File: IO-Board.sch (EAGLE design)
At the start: 59 parts, among them IC1 PCF8574P, IC2 PCF8574P

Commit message: IO-Board angepasst, 433MHz-Sender hinzugefügt
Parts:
- added +3V3.1, +3V3.2, +3V3.3, +3V3.4, 1WIRE.1, 1WIRE.2, 1WIRE.3, 1WIRE.4, GND.1, GND.2, GND.3, GND.4, GNDIO.1, GNDIO.10, GNDIO.11, GNDIO.12, GNDIO.13, GNDIO.14, GNDIO.15, GNDIO.16, GNDIO.17, GNDIO.18, GNDIO.19, GNDIO.2, GNDIO.20, GNDIO.21, GNDIO.22, GNDIO.23, GNDIO.24, GNDIO.3, GNDIO.4, GNDIO.5, GNDIO.6, GNDIO.7, GNDIO.8, GNDIO.9, GPIO_06, GPIO_12, GPIO_13, GPIO_16, GPIO_17, GPIO_18, GPIO_19, GPIO_20, GPIO_21, GPIO_22, GPIO_23, IC3_INT, IC4_INT, J1.1, J1.2, J1.3, J1.4, J1.5, J1.6, J1.7, J1.8, J2.1, J2.2, J2.3, J2.4, J2.5, J2.6, J2.7, J2.8, J3.1, J3.2, J3.3, J3.4, J3.5, J3.6, J3.7, J3.8, J4.1, J4.2, J4.3, J4.4, J4.5, J4.6, J4.7, J4.8, SV2.1, SV2.10, SV2.2, SV2.3, SV2.4, SV2.5, SV2.6, SV2.7, SV2.8, SV2.9, SV3.1, SV3.10, SV3.2, SV3.3, SV3.4, SV3.5, SV3.6, SV3.7, SV3.8, SV3.9, TP17, TP18, TP19, TP20, TP21, TP22, TP23, TP24, TP26, TP27, TP28, TP29, TP30, TP31, TP32, TP33, VCCIO.1, VCCIO.10, VCCIO.11, VCCIO.12, VCCIO.13, VCCIO.14, VCCIO.15, VCCIO.16, VCCIO.17, VCCIO.18, VCCIO.19, VCCIO.2, VCCIO.20, VCCIO.21, VCCIO.22, VCCIO.23, VCCIO.24, VCCIO.3, VCCIO.4, VCCIO.5, VCCIO.6, VCCIO.7, VCCIO.8, VCCIO.9: TPPAD1-13, testpad:TPPAD1-13
- added C3, C4: 100nF, rcl:C-EU025-025X050
- added IC3, IC4: PCF8574P, micro-philips:PCF8574P
- added J1, J2, J3, J4: (no value), con-amp:555141-1
- added J5: J7MM, jumper:J7MM
- added OK1, OK10, OK11, OK12, OK13, OK14, OK15, OK16, OK17, OK18, OK19, OK2, OK20, OK21, OK22, OK23, OK24, OK25, OK26, OK27, OK28, OK29, OK3, OK30, OK31, OK32, OK4, OK5, OK6, OK7, OK8, OK9: CNY17SMD, homepi:CNY17SMD
- added R17, R20, R23, R26, R29, R32, R35, R38, R41, R44, R47: 10k, rcl:R-EU_0204/2V
- added R18, R21, R24, R27, R30, R33, R36, R39, R42, R45, R48: 4k7, rcl:R-EU_0204/2V
- added R19, R22, R25, R28, R31, R34, R37, R40, R43, R46, R49, R50, R51, R52, R53, R54, R55, R56, R57, R58, R59, R60, R61, R62, R63, R64: 330, rcl:R-EU_0204/2V
- added R65, R66: J5MM, jumper:J5MM
- added SJ10, SJ11, SJ12, SJ7, SJ8, SJ9: (no value), jumper:SJ2W
- added SV2, SV3: (no value), con-harting-ml:ML10
- R1, R10, R13, R16, R4, R7: value (none) -> 330
- R11, R14, R2, R5, R8: value (none) -> 10k
- R12, R15, R3, R6, R9: value (none) -> 4k7
- T1, T10, T11, T12, T13, T14, T15, T16, T2, T3, T4, T5, T6, T7, T8, T9: value (none) -> BC337-25; device transistor:BC557C-PNP-TO92-EBC -> transistor:BC337-25-NPN-TO92-CBE
- TP1, TP10, TP11, TP12, TP13, TP14, TP15, TP16, TP2, TP3, TP4, TP5, TP6, TP7, TP8, TP9: value TPPAD1-17 -> TPPAD1-13; device testpad:TPPAD1-17 -> testpad:TPPAD1-13
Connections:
- removed net +5V: SV1.1
- new net 1WIRE: 1WIRE.1.TP, 1WIRE.2.TP, 1WIRE.3.TP, 1WIRE.4.TP, J5.2
- new net GNDIO: GNDIO.1.TP, GNDIO.10.TP, GNDIO.11.TP, GNDIO.12.TP, GNDIO.13.TP, GNDIO.14.TP, GNDIO.15.TP, GNDIO.16.TP, GNDIO.17.TP, GNDIO.18.TP, GNDIO.19.TP, GNDIO.2.TP, GNDIO.20.TP, GNDIO.21.TP, GNDIO.22.TP, GNDIO.23.TP, GNDIO.24.TP, GNDIO.3.TP, GNDIO.4.TP, GNDIO.5.TP, GNDIO.6.TP, GNDIO.7.TP, GNDIO.8.TP, GNDIO.9.TP, J1.S1, J1.S2, J2.S1, J2.S2, J3.S1, J3.S2, J4.S1, J4.S2, R11.1, R14.1, R17.1, R2.1, R20.1, R23.1, R26.1, R29.1, R32.1, R35.1, R38.1, R41.1, R44.1, R47.1, R5.1, R8.1, SV1.30, T1.E, T10.E, T11.E, T12.E, T13.E, T14.E, T15.E, T16.E, T2.E, T3.E, T4.E, T5.E, T6.E, T7.E, T8.E, T9.E
- new net IN_1.0: IC3.P0, OK17.COL
- new net IN_1.1: IC3.P1, OK18.COL
- new net IN_1.2: IC3.P2, OK19.COL
- new net IN_1.3: IC3.P3, OK20.COL
- new net IN_1.4: IC3.P4, OK21.COL
- new net IN_1.5: IC3.P5, OK22.COL
- new net IN_1.6: IC3.P6, OK23.COL
- new net IN_1.7: IC3.P7, OK24.COL
- new net IN_2.0: IC4.P0, OK25.COL
- new net IN_2.1: IC4.P1, OK26.COL
- new net IN_2.2: IC4.P2, OK27.COL
- new net IN_2.3: IC4.P3, OK28.COL
- new net IN_2.4: IC4.P4, OK29.COL
- new net IN_2.5: IC4.P5, OK30.COL
- new net IN_2.6: IC4.P6, OK31.COL
- new net IN_2.7: IC4.P7, OK32.COL
- new net N$100: OK22.A, R54.1
- new net N$101: OK22.C, TP22.TP
- new net N$102: OK23.A, R55.1
- new net N$103: OK23.C, TP23.TP
- new net N$104: OK24.A, R56.1
- new net N$105: OK24.C, TP24.TP
- new net N$106: IC3.!INT, IC3_INT.TP
- new net N$107: IC4.A0, SJ10.2
- new net N$108: IC4.A1, SJ11.2
- new net N$109: IC4.A2, SJ12.2
- new net N$110: OK25.A, R57.1
- new net N$111: OK25.C, TP26.TP
- new net N$112: OK26.A, R58.1
- new net N$113: OK26.C, TP27.TP
- new net N$114: OK27.A, R59.1
- new net N$115: OK27.C, TP28.TP
- new net N$116: OK28.A, R60.1
- new net N$117: OK28.C, TP29.TP
- new net N$118: OK29.A, R61.1
- new net N$119: OK29.C, TP30.TP
- new net N$120: OK30.A, R62.1
- new net N$121: OK30.C, TP31.TP
- new net N$122: OK31.A, R63.1
- new net N$123: OK31.C, TP32.TP
- new net N$124: OK32.A, R64.1
- new net N$125: OK32.C, TP33.TP
- new net N$126: IC4.!INT, IC4_INT.TP
- new net N$127: IC4.SDA, R65.1
- new net N$128: IC4.SCL, R66.1
- new net N$129: J3.1, J3.1.TP
- new net N$130: J3.2, J3.2.TP
- new net N$131: J3.3, J3.3.TP
- new net N$132: J3.4, J3.4.TP
- new net N$133: J3.5, J3.5.TP
- new net N$134: J3.6, J3.6.TP
- new net N$135: J3.7, J3.7.TP
- new net N$136: J3.8, J3.8.TP
- new net N$137: J4.1, J4.1.TP
- new net N$138: J4.2, J4.2.TP
- new net N$139: J4.3, J4.3.TP
- new net N$140: J4.4, J4.4.TP
- new net N$141: J4.5, J4.5.TP
- new net N$142: J4.6, J4.6.TP
- new net N$143: J4.7, J4.7.TP
- new net N$144: J4.8, J4.8.TP
- new net N$145: J5.1, SV1.7
- new net N$146: GPIO_23.TP, SV1.25
- new net N$147: GPIO_22.TP, SV1.24
- new net N$148: GPIO_21.TP, SV1.23
- new net N$149: GPIO_20.TP, SV1.22
- new net N$150: GPIO_19.TP, SV1.21
- new net N$151: GPIO_18.TP, SV1.20
- new net N$152: GPIO_17.TP, SV1.19
- new net N$153: GPIO_16.TP, SV1.18
- new net N$154: GPIO_13.TP, SV1.17
- new net N$155: GPIO_12.TP, SV1.16
- new net N$156: GPIO_06.TP, SV1.15
- new net N$157: SV2.1, SV2.1.TP
- new net N$158: SV2.2, SV2.2.TP
- new net N$159: SV2.3, SV2.3.TP
- new net N$160: SV2.4, SV2.4.TP
- new net N$161: SV2.5, SV2.5.TP
- new net N$162: SV2.6, SV2.6.TP
- new net N$163: SV2.7, SV2.7.TP
- new net N$164: SV2.8, SV2.8.TP
- new net N$165: SV2.9, SV2.9.TP
- new net N$166: SV2.10, SV2.10.TP
- new net N$167: SV3.1, SV3.1.TP
- new net N$168: SV3.2, SV3.2.TP
- new net N$169: SV3.3, SV3.3.TP
- new net N$170: SV3.4, SV3.4.TP
- new net N$171: SV3.5, SV3.5.TP
- new net N$172: SV3.6, SV3.6.TP
- new net N$173: SV3.7, SV3.7.TP
- new net N$174: SV3.8, SV3.8.TP
- new net N$175: SV3.9, SV3.9.TP
- new net N$176: SV3.10, SV3.10.TP
- new net N$28: T7.C, TP7.TP
- new net N$29: OK7.A, R19.2
- new net N$30: OK7.EMI, R20.2, R21.1
- new net N$55: R27.2, T9.B
- new net N$56: T10.C, TP10.TP
- new net N$57: OK10.A, R28.2
- new net N$58: OK10.EMI, R29.2, R30.1
- new net N$59: R30.2, T10.B
- new net N$60: T11.C, TP11.TP
- new net N$61: OK11.A, R31.2
- new net N$62: OK11.EMI, R32.2, R33.1
- new net N$63: R33.2, T11.B
- new net N$64: T12.C, TP12.TP
- new net N$65: OK12.A, R34.2
- new net N$66: OK12.EMI, R35.2, R36.1
- new net N$67: R36.2, T12.B
- new net N$68: T13.C, TP13.TP
- new net N$69: OK13.A, R37.2
- new net N$70: OK13.EMI, R38.2, R39.1
- new net N$71: R39.2, T13.B
- new net N$72: T14.C, TP14.TP
- new net N$73: OK14.A, R40.2
- new net N$74: OK14.EMI, R41.2, R42.1
- new net N$75: R42.2, T14.B
- new net N$76: T15.C, TP15.TP
- new net N$77: OK15.A, R43.2
- new net N$78: OK15.EMI, R44.2, R45.1
- new net N$79: R45.2, T15.B
- new net N$80: T16.C, TP16.TP
- new net N$81: OK16.A, R46.2
- new net N$82: OK16.EMI, R47.2, R48.1
- new net N$83: R48.2, T16.B
- new net N$87: IC3.A0, SJ7.2
- new net N$88: IC3.A1, SJ8.2
- new net N$89: IC3.A2, SJ9.2
- new net N$90: OK17.A, R49.1
- new net N$91: OK17.C, TP17.TP
- new net N$92: OK18.A, R50.1
- new net N$93: OK18.C, TP18.TP
- new net N$94: OK19.A, R51.1
- new net N$95: OK19.C, TP19.TP
- new net N$96: OK20.A, R52.1
- new net N$97: OK20.C, TP20.TP
- new net N$98: OK21.A, R53.1
- new net N$99: OK21.C, TP21.TP
- new net OUT_1.0: IC1.P0, OK1.C
- new net OUT_1.1: IC1.P1, OK2.C
- new net OUT_1.2: IC1.P2, OK3.C
- new net OUT_1.3: IC1.P3, OK4.C
- new net OUT_1.4: IC1.P4, OK5.C
- new net OUT_1.5: IC1.P5, OK6.C
- new net OUT_1.6: IC1.P6, OK7.C
- new net OUT_1.7: IC1.P7, OK8.C
- new net OUT_2.0: IC2.P0, OK9.C
- new net OUT_2.1: IC2.P1, OK10.C
- new net OUT_2.2: IC2.P2, OK11.C
- new net OUT_2.3: IC2.P3, OK12.C
- new net OUT_2.4: IC2.P4, OK13.C
- new net OUT_2.5: IC2.P5, OK14.C
- new net OUT_2.6: IC2.P6, OK15.C
- new net OUT_2.7: IC2.P7, OK16.C
- new net VCCIO: OK1.COL, OK10.COL, OK11.COL, OK12.COL, OK13.COL, OK14.COL, OK15.COL, OK16.COL, OK2.COL, OK3.COL, OK4.COL, OK5.COL, OK6.COL, OK7.COL, OK8.COL, OK9.COL, R49.2, R50.2, R51.2, R52.2, R53.2, R54.2, R55.2, R56.2, R57.2, R58.2, R59.2, R60.2, R61.2, R62.2, R63.2, R64.2, SV1.31, VCCIO.1.TP, VCCIO.10.TP, VCCIO.11.TP, VCCIO.12.TP, VCCIO.13.TP, VCCIO.14.TP, VCCIO.15.TP, VCCIO.16.TP, VCCIO.17.TP, VCCIO.18.TP, VCCIO.19.TP, VCCIO.2.TP, VCCIO.20.TP, VCCIO.21.TP, VCCIO.22.TP, VCCIO.23.TP, VCCIO.24.TP, VCCIO.3.TP, VCCIO.4.TP, VCCIO.5.TP, VCCIO.6.TP, VCCIO.7.TP, VCCIO.8.TP, VCCIO.9.TP
- net +3V3: now also +3V3.1.TP, +3V3.2.TP, +3V3.3.TP, +3V3.4.TP, C3.1, C4.1, IC3.VDD, IC4.VDD, R1.1, R10.1, R13.1, R16.1, R19.1, R22.1, R25.1, R28.1, R31.1, R34.1, R37.1, R4.1, R40.1, R43.1, R46.1, R7.1, SJ10.3, SJ11.3, SJ12.3, SJ7.3, SJ8.3, SJ9.3
- net GND: now also C3.2, C4.2, GND.1.TP, GND.2.TP, GND.3.TP, GND.4.TP, IC3.VSS, IC4.VSS, OK17.EMI, OK18.EMI, OK19.EMI, OK20.EMI, OK21.EMI, OK22.EMI, OK23.EMI, OK24.EMI, OK25.EMI, OK26.EMI, OK27.EMI, OK28.EMI, OK29.EMI, OK30.EMI, OK31.EMI, OK32.EMI, SJ10.1, SJ11.1, SJ12.1, SJ7.1, SJ8.1, SJ9.1; no longer T1.C, T10.C, T11.C, T12.C, T13.C, T14.C, T15.C, T16.C, T2.C, T3.C, T4.C, T5.C, T6.C, T7.C, T8.C, T9.C
- net N$10: now also OK2.EMI, R5.2, R6.1; no longer T3.E, TP3.TP
- net N$11: now also R6.2, T2.B; no longer T4.E, TP4.TP
- net N$12: now also T3.C, TP3.TP; no longer R6.2, T6.B
- net N$13: now also OK3.A, R7.2; no longer R5.2, T5.B
- net N$14: now also OK3.EMI, R8.2, R9.1; no longer R4.2, T4.B
- net N$15: now also R9.2; no longer R3.2
- net N$16: now also T4.C, TP4.TP; no longer T7.E, TP7.TP
- net N$17: now also OK4.A, R10.2; no longer T8.E, TP8.TP
- net N$18: now also OK4.EMI, R11.2, R12.1; no longer R8.2, T8.B
- net N$19: now also R12.2, T4.B; no longer R7.2, T7.B
- net N$20: now also T5.C, TP5.TP; no longer IC1.P0, R1.1
- net N$21: now also OK5.A, R13.2; no longer IC1.P1, R2.1
- net N$22: now also OK5.EMI, R14.2, R15.1; no longer IC1.P2, R3.1
- net N$23: now also R15.2, T5.B; no longer IC1.P3, R4.1
- net N$24: now also T6.C, TP6.TP; no longer IC1.P4, R5.1
- net N$25: now also OK6.A, R16.2; no longer IC1.P5, R6.1
- net N$26: now also OK6.EMI, R17.2, R18.1; no longer IC1.P6, R7.1
- net N$27: now also R18.2, T6.B; no longer IC1.P7, R8.1
- net N$31: now also R21.2, T7.B; no longer T9.E, TP9.TP
- net N$32: now also T8.C, TP8.TP; no longer T10.E, TP10.TP
- net N$33: now also OK8.A, R22.2; no longer R10.2, T10.B
- net N$34: now also OK8.EMI, R23.2, R24.1; no longer R9.2, T9.B
- net N$35: now also R24.2, T8.B; no longer T11.E, TP11.TP
- net N$36: now also J1.1, J1.1.TP; no longer T12.E, TP12.TP
- net N$37: now also J1.2, J1.2.TP; no longer R12.2, T12.B
- net N$38: now also J1.3, J1.3.TP; no longer R11.2, T11.B
- net N$39: now also J1.4, J1.4.TP; no longer T13.E, TP13.TP
- net N$4: now also T1.C; no longer T1.E
- net N$40: now also J1.5, J1.5.TP; no longer T14.E, TP14.TP
- net N$41: now also J1.6, J1.6.TP; no longer R14.2, T14.B
- net N$42: now also J1.7, J1.7.TP; no longer R13.2, T13.B
- net N$43: now also J1.8, J1.8.TP; no longer T15.E, TP15.TP
- net N$44: now also J2.1, J2.1.TP; no longer T16.E, TP16.TP
- net N$45: now also J2.2, J2.2.TP; no longer R16.2, T16.B
- net N$46: now also J2.3, J2.3.TP; no longer R15.2, T15.B
- net N$47: now also J2.4, J2.4.TP; no longer IC2.P0, R9.1
- net N$48: now also J2.5, J2.5.TP; no longer IC2.P1, R10.1
- net N$49: now also J2.6, J2.6.TP; no longer IC2.P2, R11.1
- net N$5: now also OK1.A, R1.2; no longer T2.E, TP2.TP
- net N$50: now also J2.7, J2.7.TP; no longer IC2.P3, R12.1
- net N$51: now also J2.8, J2.8.TP; no longer IC2.P4, R13.1
- net N$52: now also T9.C, TP9.TP; no longer IC2.P5, R14.1
- net N$53: now also OK9.A, R25.2; no longer IC2.P6, R15.1
- net N$54: now also OK9.EMI, R26.2, R27.1; no longer IC2.P7, R16.1
- net N$6: now also OK1.EMI, R2.2, R3.1; no longer T5.E, TP5.TP
- net N$7: now also R3.2, T1.B; no longer T6.E, TP6.TP
- net N$8: now also T2.C, TP2.TP; no longer R2.2, T2.B
- net N$9: now also OK2.A, R4.2; no longer R1.2, T1.B
- net SCL: now also IC3.SCL, R66.2
- net SDA: now also IC3.SDA, R65.2

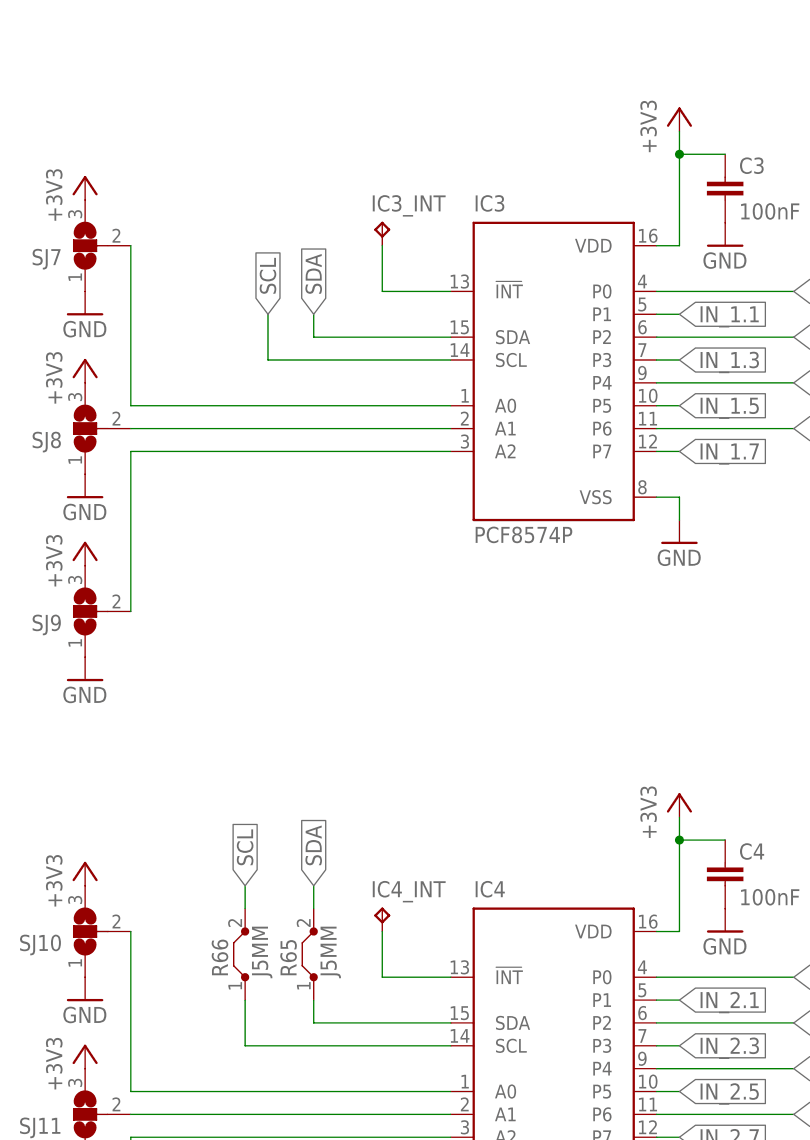
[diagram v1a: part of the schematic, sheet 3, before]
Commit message: IO-Board und IO-Board-2 Anpassungen
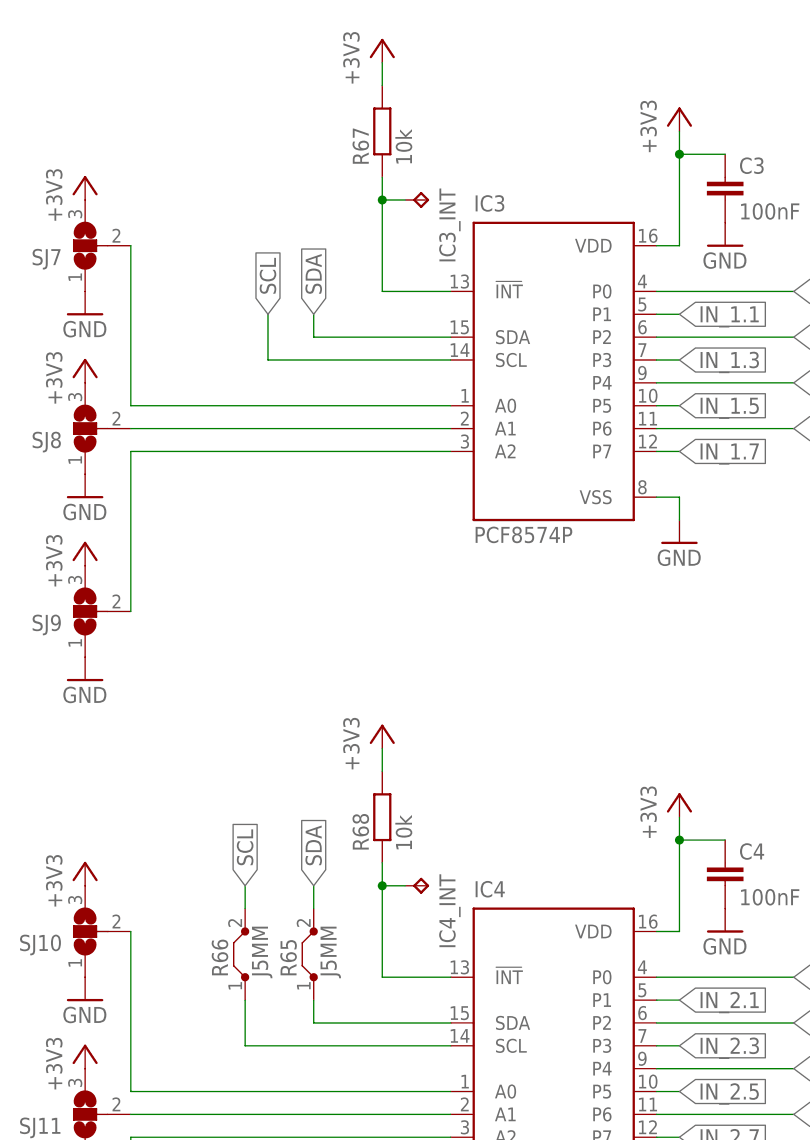
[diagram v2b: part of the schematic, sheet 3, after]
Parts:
- added GPIO_24: TPPAD1-13, testpad:TPPAD1-13
- added R67, R68: 10k, rcl:R-EU_0204/2V
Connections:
- new net N$177: GPIO_24.TP, SV1.26
- net +3V3: now also R67.2, R68.2
- net N$106: now also R67.1
- net N$126: now also R68.1
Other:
- moved on the sheet: IC3_INT, IC4_INT
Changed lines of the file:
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@@
 <part name="VCCIO.23" library="testpad" deviceset="TP" device="PAD1-13" value="TPPAD1-13"/>
 <part name="VCCIO.24" library="testpad" deviceset="TP" device="PAD1-13" value="TPPAD1-13"/>
+<part name="GPIO_24" library="testpad" deviceset="TP" device="PAD1-13" value="TPPAD1-13"/>
+<part name="R67" library="rcl" deviceset="R-EU_" device="0204/2V" value="10k"/>
+<part name="+3V34" library="supply1" deviceset="+3V3" device="" value="+3V3"/>
+<part name="R68" library="rcl" deviceset="R-EU_" device="0204/2V" value="10k"/>
+<part name="+3V35" library="supply1" deviceset="+3V3" device="" value="+3V3"/>
 </parts>
 <sheets>
@@
 <instance part="VCCIO.23" gate="G$1" x="261.62" y="93.98"/>
 <instance part="VCCIO.24" gate="G$1" x="274.32" y="93.98"/>
+<instance part="GPIO_24" gate="G$1" x="30.48" y="68.58" smashed="yes" rot="R270">
+<attribute name="NAME" x="31.75" y="67.31" size="1.778" layer="95"/>
+<attribute name="TP_SIGNAL_NAME" x="29.21" y="67.31" size="1.778" layer="97" rot="R270"/>
+</instance>
 </instances>
 <busses>
@@
 </segment>
 </net>
+<net name="N$177" class="0">
+<segment>
+<pinref part="SV1" gate="1" pin="26"/>
+<pinref part="GPIO_24" gate="G$1" pin="TP"/>
+<wire x1="20.32" y1="68.58" x2="27.94" y2="68.58" width="0.1524" layer="91"/>
+</segment>
+</net>
 </nets>
 </sheet>
@@
 <instance part="GND59" gate="1" x="281.94" y="88.9"/>
 <instance part="TP24" gate="G$1" x="309.88" y="93.98" rot="R270"/>
-<instance part="IC3_INT" gate="G$1" x="35.56" y="129.54"/>
+<instance part="IC3_INT" gate="G$1" x="40.64" y="132.08" rot="R270"/>
 <instance part="IC4" gate="G$1" x="53.34" y="38.1"/>
 <instance part="+3V28" gate="G$1" x="68.58" y="66.04"/>
@@
 <instance part="GND72" gate="1" x="287.02" y="12.7"/>
 <instance part="TP33" gate="G$1" x="314.96" y="17.78" rot="R270"/>
-<instance part="IC4_INT" gate="G$1" x="35.56" y="53.34"/>
+<instance part="IC4_INT" gate="G$1" x="40.64" y="55.88" rot="R270"/>
 <instance part="R65" gate="1" x="27.94" y="48.26" rot="R90"/>
 <instance part="R66" gate="1" x="20.32" y="48.26" rot="R90"/>
+<instance part="R67" gate="G$1" x="35.56" y="139.7" rot="R90"/>
+<instance part="+3V34" gate="G$1" x="35.56" y="149.86"/>
+<instance part="R68" gate="G$1" x="35.56" y="63.5" rot="R90"/>
+<instance part="+3V35" gate="G$1" x="35.56" y="73.66"/>
 </instances>
 <busses>
@@
 <pinref part="+3V31" gate="G$1" pin="+3V3"/>
 </segment>
+<segment>
+<pinref part="R67" gate="G$1" pin="2"/>
+<pinref part="+3V34" gate="G$1" pin="+3V3"/>
+<wire x1="35.56" y1="144.78" x2="35.56" y2="147.32" width="0.1524" layer="91"/>
+</segment>
+<segment>
+<pinref part="R68" gate="G$1" pin="2"/>
+<pinref part="+3V35" gate="G$1" pin="+3V3"/>
+<wire x1="35.56" y1="68.58" x2="35.56" y2="71.12" width="0.1524" layer="91"/>
+</segment>
 </net>
 <net name="GND" class="0">
@@
 <pinref part="IC3_INT" gate="G$1" pin="TP"/>
 <wire x1="43.18" y1="121.92" x2="35.56" y2="121.92" width="0.1524" layer="91"/>
-<wire x1="35.56" y1="121.92" x2="35.56" y2="127" width="0.1524" layer="91"/>
+<wire x1="35.56" y1="121.92" x2="35.56" y2="132.08" width="0.1524" layer="91"/>
+<wire x1="35.56" y1="132.08" x2="38.1" y2="132.08" width="0.1524" layer="91"/>
+<pinref part="R67" gate="G$1" pin="1"/>
+<wire x1="35.56" y1="132.08" x2="35.56" y2="134.62" width="0.1524" layer="91"/>
+<junction x="35.56" y="132.08"/>
 </segment>
 </net>
@@
 <pinref part="IC4_INT" gate="G$1" pin="TP"/>
 <wire x1="43.18" y1="45.72" x2="35.56" y2="45.72" width="0.1524" layer="91"/>
-<wire x1="35.56" y1="45.72" x2="35.56" y2="50.8" width="0.1524" layer="91"/>
+<wire x1="35.56" y1="45.72" x2="35.56" y2="55.88" width="0.1524" layer="91"/>
+<wire x1="35.56" y1="55.88" x2="38.1" y2="55.88" width="0.1524" layer="91"/>
+<pinref part="R68" gate="G$1" pin="1"/>
+<wire x1="35.56" y1="55.88" x2="35.56" y2="58.42" width="0.1524" layer="91"/>
+<junction x="35.56" y="55.88"/>
 </segment>
 </net>

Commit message: Schaltpläne aufgehübscht zur Veröffentlichung
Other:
- note added: "Ausgänge"
- note added: "Eingänge"
- note added: "HomePi - IO-Platine Rev. 2016/08 Ausgänge Teil 1"
- note added: "HomePi - IO-Platine Rev. 2016/08 Ausgänge Teil 2"
- note added: "HomePi - IO-Platine Rev. 2016/08 Eingänge"
- note added: "HomePi - IO-Platine Rev. 2016/08 ICs"
- note added: "HomePi - IO-Platine Rev. 2016/08 Verbinder"
